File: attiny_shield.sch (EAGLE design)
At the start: 11 parts, among them IC1 TINY13-20PU

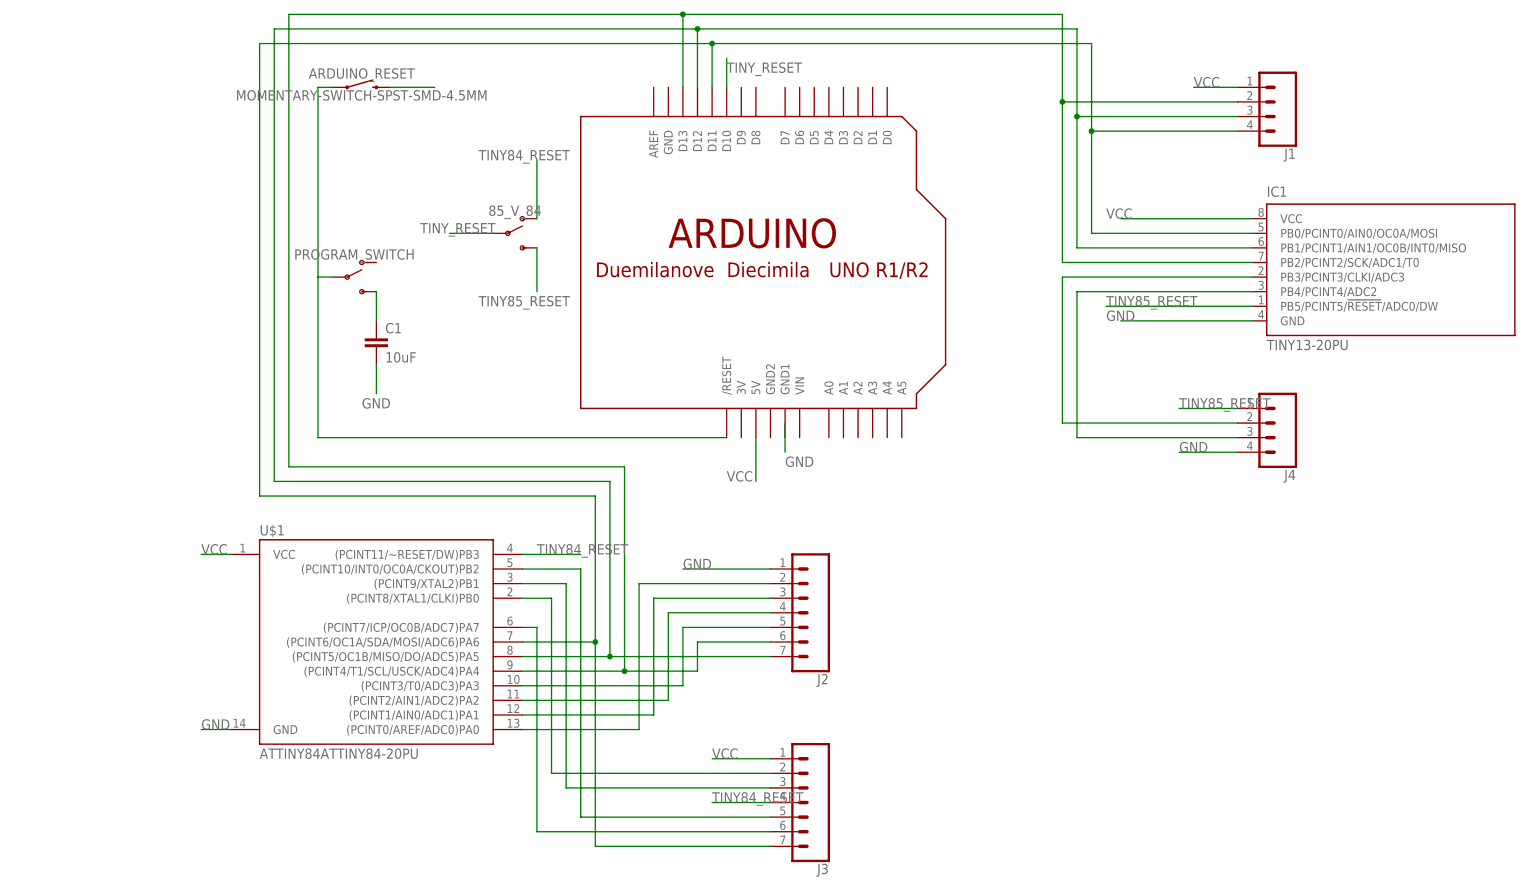
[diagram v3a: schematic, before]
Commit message: independent resets
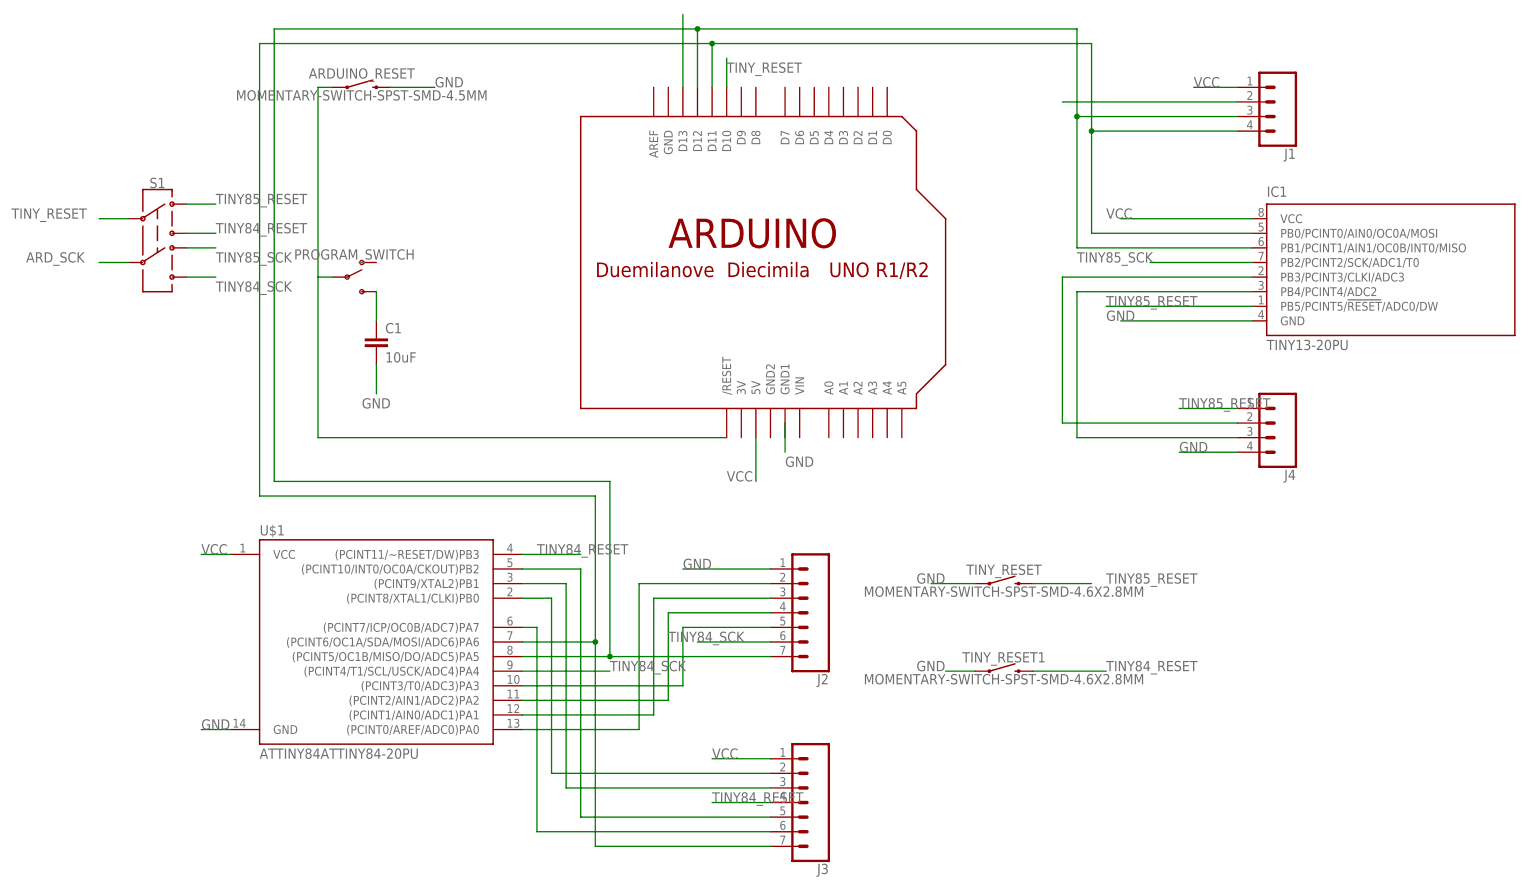
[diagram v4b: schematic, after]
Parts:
- removed 85_V_84: (no value), SparkFun-Switches:SWITCH-SPDT-SMD-AYZ0202
- added S1: (no value), SparkFun-Switches:SWITCH-DPDT-SMD-AYZ0202
- added TINY_RESET, TINY_RESET1: MOMENTARY-SWITCH-SPST-SMD-4.6X2.8MM, SparkFun-Switches:MOMENTARY-SWITCH-SPST-SMD-4.6X2.8MM
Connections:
- removed net N$1: IC1.PB2/PCINT2/SCK/ADC1/T0, J1.2, J2.6, U$1.(PCINT4/T1/SCL/USCK/ADC4)PA4, U$2.D13
- new net ARD_SCK: S1.5, U$2.D13
- new net TINY84_SCK: J2.6, S1.6, U$1.(PCINT4/T1/SCL/USCK/ADC4)PA4
- new net TINY85_SCK: IC1.PB2/PCINT2/SCK/ADC1/T0, J1.2, S1.4
- net GND: now also TINY_RESET.1, TINY_RESET1.1
- net TINY84_RESET: now also S1.3, TINY_RESET1.2; no longer 85_V_84.O
- net TINY85_RESET: now also S1.1, TINY_RESET.2; no longer 85_V_84.S
- net TINY_RESET: now also S1.2; no longer 85_V_84.P
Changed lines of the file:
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@@
 <part name="U$2" library="adafruit" deviceset="ARDUINO" device="-NODIM"/>
 <part name="PROGRAM_SWITCH" library="SparkFun-Switches" deviceset="SWITCH-SPDT" device="-SMD-AYZ0202"/>
-<part name="85_V_84" library="SparkFun-Switches" deviceset="SWITCH-SPDT" device="-SMD-AYZ0202"/>
 <part name="J2" library="SparkFun-Connectors" deviceset="CONN_07" device=""/>
 <part name="J3" library="SparkFun-Connectors" deviceset="CONN_07" device=""/>
@@
 <part name="C1" library="SparkFun-Capacitors" deviceset="10UF" device="-0805-10V-10%" value="10uF"/>
 <part name="ARDUINO_RESET" library="SparkFun-Switches" deviceset="MOMENTARY-SWITCH-SPST" device="-SMD-4.5MM"/>
+<part name="TINY_RESET" library="SparkFun-Switches" deviceset="MOMENTARY-SWITCH-SPST" device="-SMD-4.6X2.8MM" value="MOMENTARY-SWITCH-SPST-SMD-4.6X2.8MM"/>
+<part name="S1" library="SparkFun-Switches" deviceset="SWITCH-DPDT" device="-SMD-AYZ0202"/>
+<part name="TINY_RESET1" library="SparkFun-Switches" deviceset="MOMENTARY-SWITCH-SPST" device="-SMD-4.6X2.8MM" value="MOMENTARY-SWITCH-SPST-SMD-4.6X2.8MM"/>
 </parts>
 <sheets>
@@
 <instance part="U$2" gate="G$1" x="53.34" y="119.38"/>
 <instance part="PROGRAM_SWITCH" gate="1" x="-10.16" y="114.3"/>
-<instance part="85_V_84" gate="1" x="17.78" y="121.92"/>
 <instance part="J2" gate="G$1" x="68.58" y="58.42" rot="R180"/>
 <instance part="J3" gate="G$1" x="68.58" y="25.4" rot="R180"/>
@@
 <instance part="C1" gate="G$1" x="-5.08" y="101.6"/>
 <instance part="ARDUINO_RESET" gate="G$1" x="-7.62" y="147.32"/>
+<instance part="TINY_RESET" gate="G$1" x="104.14" y="60.96"/>
+<instance part="S1" gate="G$1" x="-43.18" y="121.92"/>
+<instance part="TINY_RESET1" gate="G$1" x="104.14" y="45.72"/>
 </instances>
 <busses>
 </busses>
 <nets>
-<net name="N$1" class="0">
-<segment>
-<pinref part="U$2" gate="G$1" pin="D13"/>
-<wire x1="48.26" y1="147.32" x2="48.26" y2="160.02" width="0.1524" layer="91"/>
-<wire x1="48.26" y1="160.02" x2="-20.32" y2="160.02" width="0.1524" layer="91"/>
-<wire x1="-20.32" y1="160.02" x2="-20.32" y2="81.28" width="0.1524" layer="91"/>
-<wire x1="-20.32" y1="81.28" x2="38.1" y2="81.28" width="0.1524" layer="91"/>
-<wire x1="38.1" y1="81.28" x2="38.1" y2="45.72" width="0.1524" layer="91"/>
-<pinref part="U$1" gate="G$1" pin="(PCINT4/T1/SCL/USCK/ADC4)PA4"/>
-<wire x1="38.1" y1="45.72" x2="20.32" y2="45.72" width="0.1524" layer="91"/>
-<wire x1="48.26" y1="160.02" x2="114.3" y2="160.02" width="0.1524" layer="91"/>
-<pinref part="IC1" gate="G$1" pin="PB2/PCINT2/SCK/ADC1/T0"/>
-<wire x1="114.3" y1="160.02" x2="114.3" y2="144.78" width="0.1524" layer="91"/>
-<wire x1="114.3" y1="144.78" x2="114.3" y2="116.84" width="0.1524" layer="91"/>
-<wire x1="114.3" y1="116.84" x2="147.32" y2="116.84" width="0.1524" layer="91"/>
-<pinref part="J2" gate="G$1" pin="6"/>
-<wire x1="63.5" y1="50.8" x2="50.8" y2="50.8" width="0.1524" layer="91"/>
-<wire x1="50.8" y1="50.8" x2="50.8" y2="45.72" width="0.1524" layer="91"/>
-<wire x1="50.8" y1="45.72" x2="38.1" y2="45.72" width="0.1524" layer="91"/>
-<junction x="38.1" y="45.72"/>
-<pinref part="J1" gate="G$1" pin="2"/>
-<wire x1="144.78" y1="144.78" x2="114.3" y2="144.78" width="0.1524" layer="91"/>
-<junction x="114.3" y="144.78"/>
-<junction x="48.26" y="160.02"/>
-</segment>
-</net>
 <net name="84_5" class="0">
 <segment>
@@
 </segment>
 <segment>
-<pinref part="85_V_84" gate="1" pin="P"/>
-<wire x1="15.24" y1="121.92" x2="7.62" y2="121.92" width="0.1524" layer="91"/>
-<label x="2.54" y="121.92" size="1.778" layer="95"/>
+<pinref part="S1" gate="G$1" pin="2"/>
+<wire x1="-48.26" y1="124.46" x2="-53.34" y2="124.46" width="0.1524" layer="91"/>
+<label x="-68.58" y="124.46" size="1.778" layer="95"/>
 </segment>
 </net>
@@
 <pinref part="ARDUINO_RESET" gate="G$1" pin="2"/>
 <wire x1="-2.54" y1="147.32" x2="5.08" y2="147.32" width="0.1524" layer="91"/>
+<label x="5.08" y="147.32" size="1.778" layer="95"/>
+</segment>
+<segment>
+<pinref part="TINY_RESET" gate="G$1" pin="1"/>
+<wire x1="99.06" y1="60.96" x2="91.44" y2="60.96" width="0.1524" layer="91"/>
+<label x="88.9" y="60.96" size="1.778" layer="95"/>
+</segment>
+<segment>
+<pinref part="TINY_RESET1" gate="G$1" pin="1"/>
+<wire x1="99.06" y1="45.72" x2="93.98" y2="45.72" width="0.1524" layer="91"/>
+<label x="88.9" y="45.72" size="1.778" layer="95"/>
 </segment>
 </net>
@@
 </segment>
 <segment>
-<pinref part="85_V_84" gate="1" pin="S"/>
-<wire x1="22.86" y1="119.38" x2="22.86" y2="111.76" width="0.1524" layer="91"/>
-<label x="12.7" y="109.22" size="1.778" layer="95"/>
+<pinref part="TINY_RESET" gate="G$1" pin="2"/>
+<wire x1="109.22" y1="60.96" x2="119.38" y2="60.96" width="0.1524" layer="91"/>
+<label x="121.92" y="60.96" size="1.778" layer="95"/>
+</segment>
+<segment>
+<pinref part="S1" gate="G$1" pin="1"/>
+<wire x1="-38.1" y1="127" x2="-33.02" y2="127" width="0.1524" layer="91"/>
+<label x="-33.02" y="127" size="1.778" layer="95"/>
 </segment>
 </net>
@@
 </segment>
 <segment>
-<pinref part="85_V_84" gate="1" pin="O"/>
-<wire x1="22.86" y1="124.46" x2="22.86" y2="134.62" width="0.1524" layer="91"/>
-<label x="12.7" y="134.62" size="1.778" layer="95"/>
-</segment>
-</net>
+<pinref part="TINY_RESET1" gate="G$1" pin="2"/>
+<wire x1="109.22" y1="45.72" x2="121.92" y2="45.72" width="0.1524" layer="91"/>
+<label x="121.92" y="45.72" size="1.778" layer="95"/>
+</segment>
+<segment>
+<pinref part="S1" gate="G$1" pin="3"/>
+<wire x1="-38.1" y1="121.92" x2="-33.02" y2="121.92" width="0.1524" layer="91"/>
+<label x="-33.02" y="121.92" size="1.778" layer="95"/>
+</segment>
+</net>
+<net name="TINY85_SCK" class="0">
+<segment>
+<pinref part="IC1" gate="G$1" pin="PB2/PCINT2/SCK/ADC1/T0"/>
+<wire x1="129.54" y1="116.84" x2="147.32" y2="116.84" width="0.1524" layer="91"/>
+<label x="116.84" y="116.84" size="1.778" layer="95"/>
+</segment>
+<segment>
+<pinref part="J1" gate="G$1" pin="2"/>
+<wire x1="144.78" y1="144.78" x2="114.3" y2="144.78" width="0.1524" layer="91"/>
+</segment>
+<segment>
+<pinref part="S1" gate="G$1" pin="4"/>
+<wire x1="-38.1" y1="119.38" x2="-33.02" y2="119.38" width="0.1524" layer="91"/>
+<label x="-33.02" y="116.84" size="1.778" layer="95"/>
+</segment>
+</net>
+<net name="ARD_SCK" class="0">
+<segment>
+<pinref part="U$2" gate="G$1" pin="D13"/>
+<wire x1="48.26" y1="147.32" x2="48.26" y2="160.02" width="0.1524" layer="91"/>
+</segment>
+<segment>
+<pinref part="S1" gate="G$1" pin="5"/>
+<wire x1="-48.26" y1="116.84" x2="-53.34" y2="116.84" width="0.1524" layer="91"/>
+<label x="-66.04" y="116.84" size="1.778" layer="95"/>
+</segment>
+</net>
+<net name="TINY84_SCK" class="0">
+<segment>
+<pinref part="U$1" gate="G$1" pin="(PCINT4/T1/SCL/USCK/ADC4)PA4"/>
+<wire x1="20.32" y1="45.72" x2="35.56" y2="45.72" width="0.1524" layer="91"/>
+<label x="35.56" y="45.72" size="1.778" layer="95"/>
+</segment>
+<segment>
+<pinref part="J2" gate="G$1" pin="6"/>
+<wire x1="63.5" y1="50.8" x2="50.8" y2="50.8" width="0.1524" layer="91"/>
+<label x="45.72" y="50.8" size="1.778" layer="95"/>
+</segment>
+<segment>
+<pinref part="S1" gate="G$1" pin="6"/>
+<wire x1="-38.1" y1="114.3" x2="-33.02" y2="114.3" width="0.1524" layer="91"/>
+<label x="-33.02" y="111.76" size="1.778" layer="95"/>
+</segment>
+</net>
